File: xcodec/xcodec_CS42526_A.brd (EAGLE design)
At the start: 80 x 80 mm, 73 parts, among them J1 PINHD-3X13/90, J2 PINHD-3X9/90, J3 PINHD-3X7/90, U1 CS42526, U2 FIN1002, U3 FIN1002

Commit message: xcodec: WIP
Signed-off-by: malo <pavol.malosek@gmail.com>
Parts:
- J1: value PINHD-3X13/90 -> (none); device 25pinhead:3X13/90 -> 25pinhead:3X03/90
- RMCK: value TPTP14R -> (none); device testpad:TP14R -> 25pinhead:1X01
- moved J1 80.0 mm to (40.0, -0.03), turned to 180 degrees
- moved J3 57.5 mm to (81.3, 40.0), turned to 270 degrees
- moved J2 56.6 mm to (40.0, 80.0), turned to 0 degrees
- moved 5V0 12.2 mm to (7.66, 39.3)
- moved 3V3 11.8 mm to (10.4, 30.2)
- moved R10 10.7 mm to (30.3, 18.5), turned to 180 degrees
- moved C24 8.96 mm to (41.4, 27.2)
- moved C21 8.60 mm to (49.0, 25.4)
- moved C2 6.33 mm to (49.8, 51.9)
- moved R7 4.59 mm to (21.7, 44.5), turned to 270 degrees
- moved C11 4.55 mm to (35.2, 61.0), turned to 180 degrees
- moved C16 4.48 mm to (35.2, 55.7), turned to 0 degrees
- moved C34 4.24 mm to (32.3, 25.9)
- moved C35 4.15 mm to (34.0, 25.9)
- moved R9 4.15 mm to (14.5, 53.6), turned to 180 degrees
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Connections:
- removed net RXP7: C32.1
- new net IN_L+: J1.1, JP3.4
- new net IN_L-: J1.3, JP3.2
- new net IN_R+: J1.6, JP3.6
- new net IN_R-: J1.4, JP3.8
- new net N$6: J3.1
- new net _A1+: J3.4, JP2.6
- new net _A1-: J3.6, JP2.4
- new net _A2+: J3.10, JP2.14
- new net _A2-: J3.12, JP2.12
- new net _A3+: J3.16, JP2.22
- new net _A3-: J3.18, JP2.20
- new net _B1+: J3.7, JP2.8
- new net _B1-: J3.9, JP2.10
- new net _B2+: J3.13, JP2.16
- new net _B2-: J3.15, JP2.18
- new net _B3+: J3.19, JP2.24
- new net _B3-: J3.21, JP2.26
- new net _MUTEC: J3.3, JP2.2
- net CX_LRCK: now also J2.3
- net CX_SCLK: now also J2.1
- net CX_SDIN1: now also J2.6
- net CX_SDIN2: now also J2.4
- net CX_SDIN3: now also J2.9
- net GND: now also C32.1, J1.2, J1.5, J1.8, J2.11, J2.14, J2.17, J2.2, J2.20, J2.23, J2.26, J2.5, J2.8, J3.11, J3.14, J3.17, J3.2, J3.20, J3.5, J3.8, U$1.18, U$1.20
- net INL+: now also JP3.3; no longer JP3.1
- net INL-: now also JP3.1; no longer JP3.3
- net INT: now also J1.9
- net RMCK: now also RMCK.1; no longer RMCK.TP
- net RST_N: now also J1.7
- net RXP0: now also J2.13
- net RXP1: now also J2.18
- net RXP1_N: now also J2.21
- net RXP1_P: now also J2.19
- net RXP2: now also J2.16
- net RXP3: now also J2.22
- net RXP4: now also J2.24
- net RXP5: now also J2.25
- net RXP6: now also J2.27
- net SAI_LRCK: now also J2.12
- net SAI_SCLK: now also J2.7
- net SAI_SDOUT: now also J2.10
- net TXP0: now also J2.15
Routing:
- net +3V3: track 0.00 -> 193.1 mm, vias 0 -> 3
- net SDA: track 4.09 -> 71.4 mm, vias 0 -> 4
- net SCL: track 4.19 -> 70.3 mm, vias 0 -> 4
- net INT: track 0.00 -> 38.2 mm
- net SAI_LRCK: track 0.00 -> 37.7 mm
- net SAI_SCLK: track 0.00 -> 34.4 mm
- net +5V_CODEC: track 256.8 -> 289.8 mm
- net RST_N: track 0.00 -> 32.2 mm
- net SAI_SDOUT: track 0.00 -> 29.7 mm
- net TXP0: track 0.00 -> 26.3 mm
- net +3V3_CODEC: track 177.0 -> 155.7 mm, vias 0 -> 2
- net RXP4: track 0.00 -> 21.2 mm
- net RXP6: track 0.00 -> 20.9 mm
- net RXP1: track 0.00 -> 20.6 mm
- net _A1-: track 0.00 -> 19.3 mm
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- added copper zone on layer 1, net GND
- added copper zone on layer 16, net GND
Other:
- board text added: "A1+"
- board text added: "A1-"
- board text added: "A2+"
- board text added: "A2-"
- board text added: "A3+"
- board text added: "A3-"
- board text added: "B1+"
- board text added: "B1-"
- board text added: "B2+"
- board text added: "B2-"
- board text added: "B3+"
- board text added: "B3-"
- board text added: "IL+"
- board text added: "IL-"
- board text added: "INT"
- board text added: "IR+"
- board text added: "IR-"
- board text added: "L+"
- board text added: "L-"
- board text added: "MTC"
- board text added: "MUTEC"
- board text added: "R+"
- board text added: "R-"
- board text added: "RST_N"
- board text added: "SCL"
- board text added: "SDA"

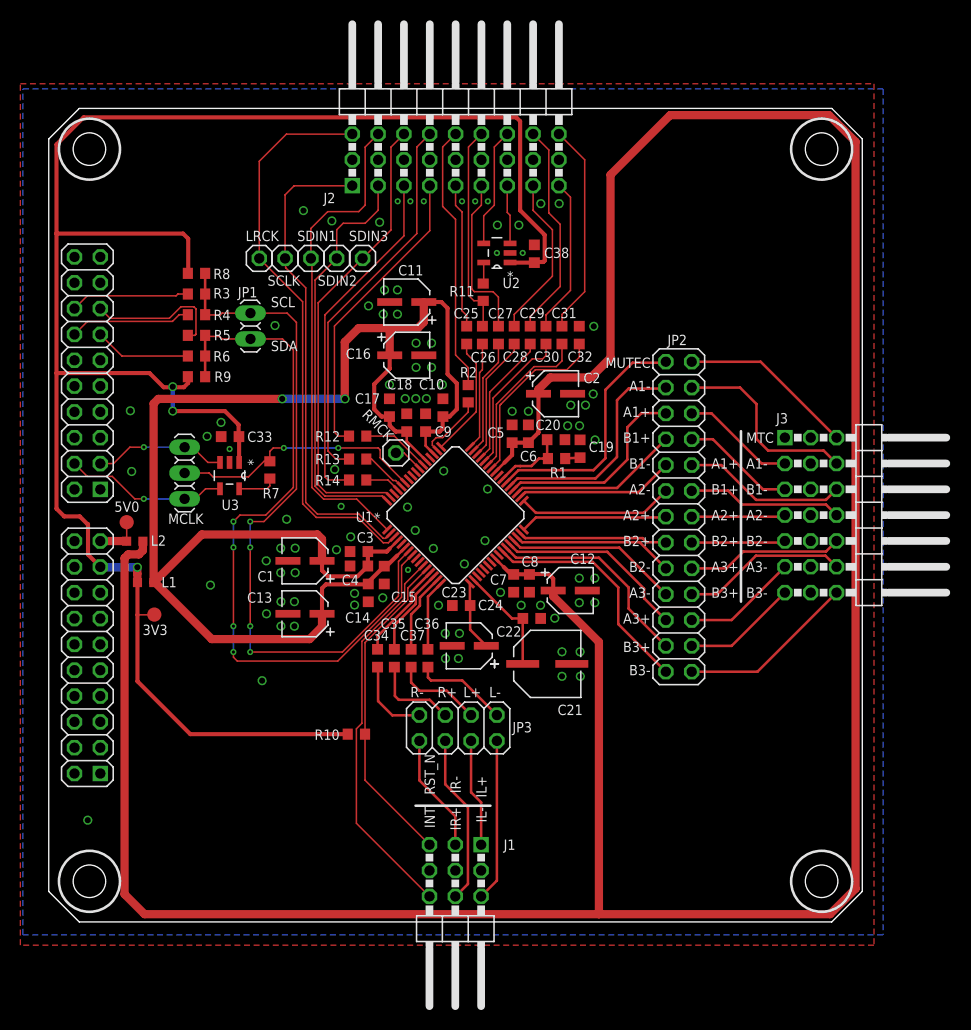
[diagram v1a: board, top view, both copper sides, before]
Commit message: xcodec: finished PCB.
Signed-off-by: malo <pavol.malosek@gmail.com>
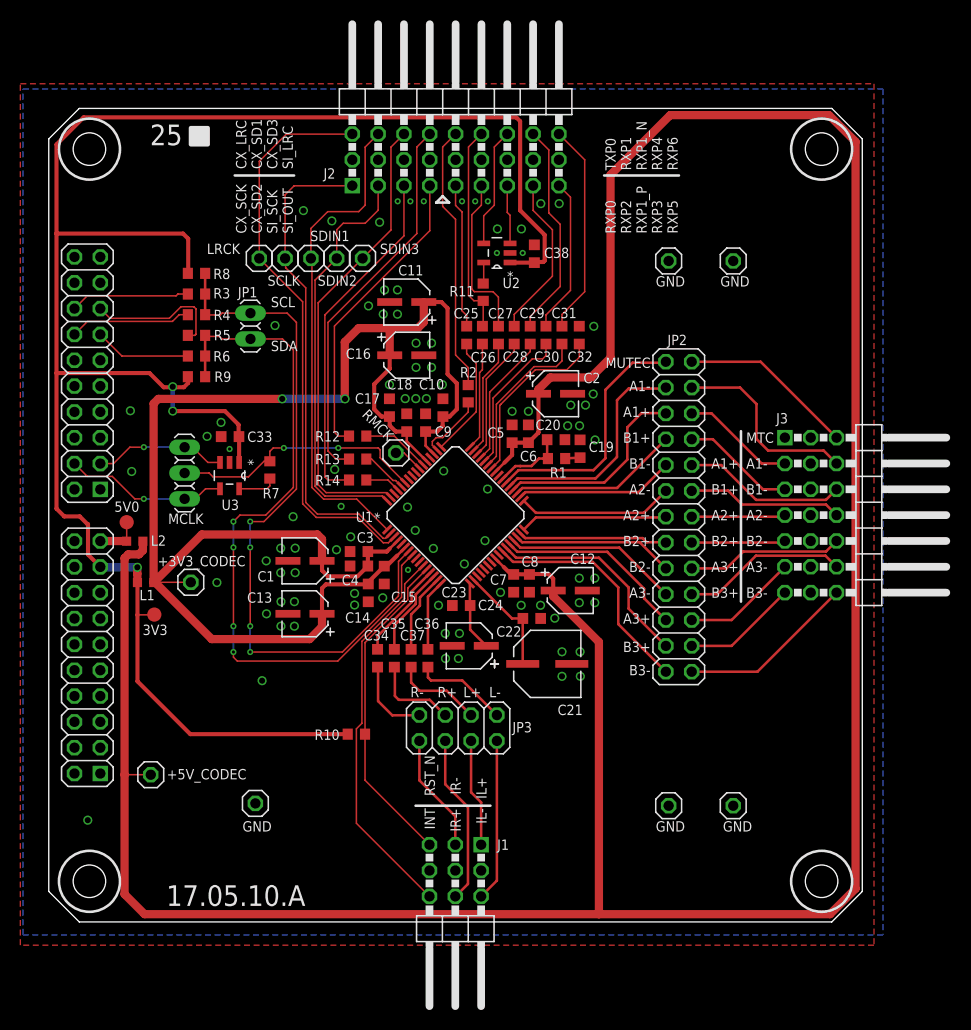
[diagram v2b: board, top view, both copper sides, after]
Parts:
- added +3V3_CODEC, +5V_CODEC, GND_0, GND_1, GND_2, GND_3, GND_4: (no value), 25pinhead:1X01
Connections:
- net +3V3_CODEC: now also +3V3_CODEC.1
- net +5V_CODEC: now also +5V_CODEC.1
- net GND: now also GND_0.1, GND_1.1, GND_2.1, GND_3.1, GND_4.1
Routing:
- net +3V3_CODEC: track 155.7 -> 159.2 mm
- net +5V_CODEC: track 289.8 -> 292.4 mm
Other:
- board text added: "17.05.10.A"
- board text added: "25"
- board text added: "CX_LRC"
- board text added: "CX_SCK"
- board text added: "CX_SD1"
- board text added: "CX_SD2"
- board text added: "CX_SD3"
- board text added: "GND"
- board text added: "RXP0"
- board text added: "RXP1"
- board text added: "RXP1_N"
- board text added: "RXP1_P"
- board text added: "RXP2"
- board text added: "RXP3"
- board text added: "RXP4"
- board text added: "RXP5"
- board text added: "RXP6"
- board text added: "SI_LRC"
- board text added: "SI_OUT"
- board text added: "SI_SCK"
- board text added: "TXP0"
